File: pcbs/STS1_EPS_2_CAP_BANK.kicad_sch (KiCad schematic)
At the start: 16 parts

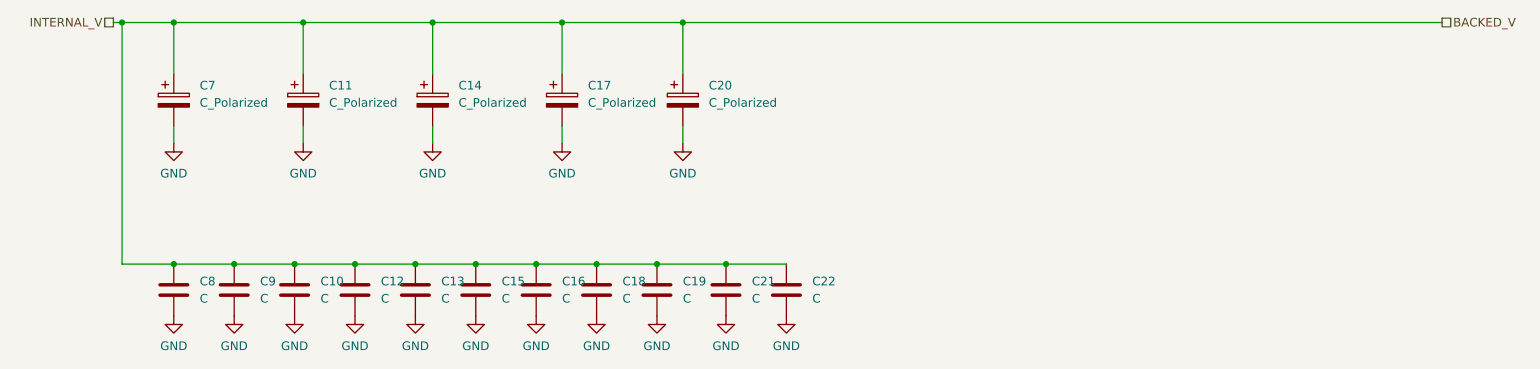
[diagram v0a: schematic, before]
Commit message: Added values to the capacitors of the capacitor bank.
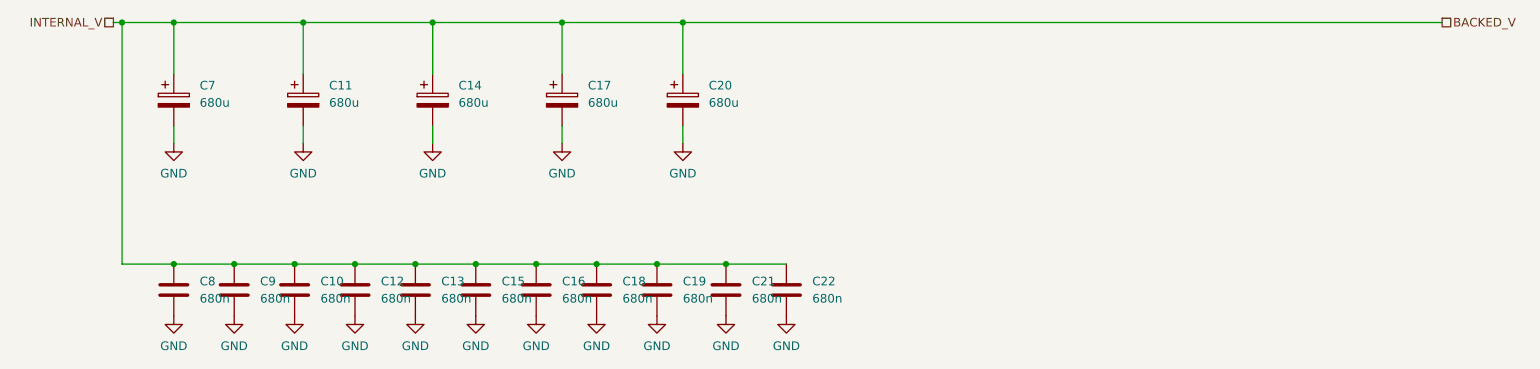
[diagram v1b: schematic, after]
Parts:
- C10, C12, C13, C15, C16, C18, C19, C21, C22, C8, C9: value C -> 680n
- C11, C14, C17, C20, C7: value C_Polarized -> 680u
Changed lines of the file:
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@@
 			)
 		)
-		(property "Value" "C"
+		(property "Value" "680n"
 			(at 96.52 68.5799 0)
 			(effects
@@
 			)
 		)
-		(property "Value" "C"
+		(property "Value" "680n"
 			(at 78.74 68.5799 0)
 			(effects
@@
 			)
 		)
-		(property "Value" "C"
+		(property "Value" "680n"
 			(at 114.3 68.5799 0)
 			(effects
@@
 			)
 		)
-		(property "Value" "C"
+		(property "Value" "680n"
 			(at 87.63 68.5799 0)
 			(effects
@@
 			)
 		)
-		(property "Value" "C_Polarized"
+		(property "Value" "680u"
 			(at 62.23 39.7509 0)
 			(effects
@@
 			)
 		)
-		(property "Value" "C_Polarized"
+		(property "Value" "680u"
 			(at 43.18 39.7509 0)
 			(effects
@@
 			)
 		)
-		(property "Value" "C"
+		(property "Value" "680n"
 			(at 133.35 68.5799 0)
 			(effects
@@
 			)
 		)
-		(property "Value" "C_Polarized"
+		(property "Value" "680u"
 			(at 100.33 39.7509 0)
 			(effects
@@
 			)
 		)
-		(property "Value" "C"
+		(property "Value" "680n"
 			(at 43.18 68.5799 0)
 			(effects
@@
 			)
 		)
-		(property "Value" "C_Polarized"
+		(property "Value" "680u"
 			(at 81.28 39.7509 0)
 			(effects
@@
 			)
 		)
-		(property "Value" "C"
+		(property "Value" "680n"
 			(at 105.41 68.5799 0)
 			(effects
@@
 			)
 		)
-		(property "Value" "C_Polarized"
+		(property "Value" "680u"
 			(at 118.11 39.7509 0)
 			(effects
@@
 			)
 		)
-		(property "Value" "C"
+		(property "Value" "680n"
 			(at 124.46 68.5799 0)
 			(effects
@@
 			)
 		)
-		(property "Value" "C"
+		(property "Value" "680n"
 			(at 60.96 68.5799 0)
 			(effects
@@
 			)
 		)
-		(property "Value" "C"
+		(property "Value" "680n"
 			(at 69.85 68.5799 0)
 			(effects
@@
 			)
 		)
-		(property "Value" "C"
+		(property "Value" "680n"
 			(at 52.07 68.5799 0)
 			(effects

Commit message: Added more part numbers.
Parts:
- C10, C12, C13, C15, C16, C18, C19, C21, C22, C8, C9: Part Nr. (none) -> C0805T684K5RCLTM
- C11, C14, C17, C20, C7: Part Nr. (none) -> TPSE687M010R0150V
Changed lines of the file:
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@@
+			)
+		)
+		(property "Part Nr." "C0805T684K5RCLTM"
+			(at 92.71 67.31 0)
+			(effects
+				(font
+					(size 1.27 1.27)
+				)
+				(hide yes)
 			)
 		)
@@
 			)
 		)
+		(property "Part Nr." "C0805T684K5RCLTM"
+			(at 74.93 67.31 0)
+			(effects
+				(font
+					(size 1.27 1.27)
+				)
+				(hide yes)
+			)
+		)
 		(pin "1"
 		)
@@
 			)
 		)
+		(property "Part Nr." "C0805T684K5RCLTM"
+			(at 110.49 67.31 0)
+			(effects
+				(font
+					(size 1.27 1.27)
+				)
+				(hide yes)
+			)
+		)
 		(pin "1"
 		)
@@
 			)
 		)
+		(property "Part Nr." "C0805T684K5RCLTM"
+			(at 83.82 67.31 0)
+			(effects
+				(font
+					(size 1.27 1.27)
+				)
+				(hide yes)
+			)
+		)
 		(pin "1"
 		)
@@
 			)
 		)
+		(property "Part Nr." "TPSE687M010R0150V"
+			(at 58.42 39.37 0)
+			(effects
+				(font
+					(size 1.27 1.27)
+				)
+				(hide yes)
+			)
+		)
 		(pin "1"
 		)
@@
 			)
 		)
+		(property "Part Nr." "TPSE687M010R0150V"
+			(at 39.37 39.37 0)
+			(effects
+				(font
+					(size 1.27 1.27)
+				)
+				(hide yes)
+			)
+		)
 		(pin "1"
 		)
@@
 			)
 		)
+		(property "Part Nr." "C0805T684K5RCLTM"
+			(at 129.54 67.31 0)
+			(effects
+				(font
+					(size 1.27 1.27)
+				)
+				(hide yes)
+			)
+		)
 		(pin "1"
 		)
@@
 			)
 		)
+		(property "Part Nr." "TPSE687M010R0150V"
+			(at 96.52 39.37 0)
+			(effects
+				(font
+					(size 1.27 1.27)
+				)
+				(hide yes)
+			)
+		)
 		(pin "1"
 		)
@@
 			)
 		)
+		(property "Part Nr." "C0805T684K5RCLTM"
+			(at 39.37 67.31 0)
+			(effects
+				(font
+					(size 1.27 1.27)
+				)
+				(hide yes)
+			)
+		)
 		(pin "1"
 		)
@@
 			)
 		)
+		(property "Part Nr." "TPSE687M010R0150V"
+			(at 77.47 39.37 0)
+			(effects
+				(font
+					(size 1.27 1.27)
+				)
+				(hide yes)
+			)
+		)
 		(pin "1"
 		)
@@
 			)
 		)
+		(property "Part Nr." "C0805T684K5RCLTM"
+			(at 101.6 67.31 0)
+			(effects
+				(font
+					(size 1.27 1.27)
+				)
+				(hide yes)
+			)
+		)
 		(pin "1"
 		)
@@
 			)
 		)
+		(property "Part Nr." "TPSE687M010R0150V"
+			(at 114.3 39.37 0)
+			(effects
+				(font
+					(size 1.27 1.27)
+				)
+				(hide yes)
+			)
+		)
 		(pin "1"
 		)
@@
 			)
 		)
+		(property "Part Nr." "C0805T684K5RCLTM"
+			(at 120.65 67.31 0)
+			(effects
+				(font
+					(size 1.27 1.27)
+				)
+				(hide yes)
+			)
+		)
 		(pin "1"
 		)
@@
 			)
 		)
+		(property "Part Nr." "C0805T684K5RCLTM"
+			(at 57.15 67.31 0)
+			(effects
+				(font
+					(size 1.27 1.27)
+				)
+				(hide yes)
+			)
+		)
 		(pin "1"
 		)
@@
 			)
 		)
+		(property "Part Nr." "C0805T684K5RCLTM"
+			(at 66.04 67.31 0)
+			(effects
+				(font
+					(size 1.27 1.27)
+				)
+				(hide yes)
+			)
+		)
 		(pin "1"
 		)
@@
 			(at 48.26 67.31 0)
 			(effects
+				(font
+					(size 1.27 1.27)
+				)
+				(hide yes)
+			)
+		)
+		(property "Part Nr." "C0805T684K5RCLTM"
+			(at 48.26 67.31 0)
+			(effects
